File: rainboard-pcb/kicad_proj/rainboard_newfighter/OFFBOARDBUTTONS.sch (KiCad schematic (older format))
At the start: 12 parts, among them J10 Conn_01x02_Female, J11 Conn_01x02_Female, J12 Conn_01x02_Female, J13 Conn_01x02_Female, J14 Conn_01x02_Female, J15 Conn_01x02_Female, J16 Conn_01x02_Female, J17 Conn_01x02_Female, J18 Conn_01x02_Female, J19 Conn_01x02_Female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

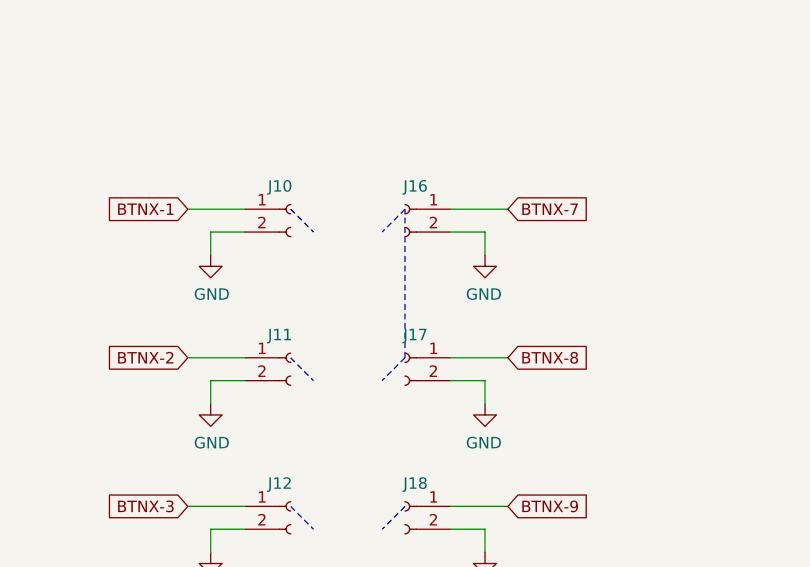
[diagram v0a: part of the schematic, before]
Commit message: Changes Micro USB to USB B
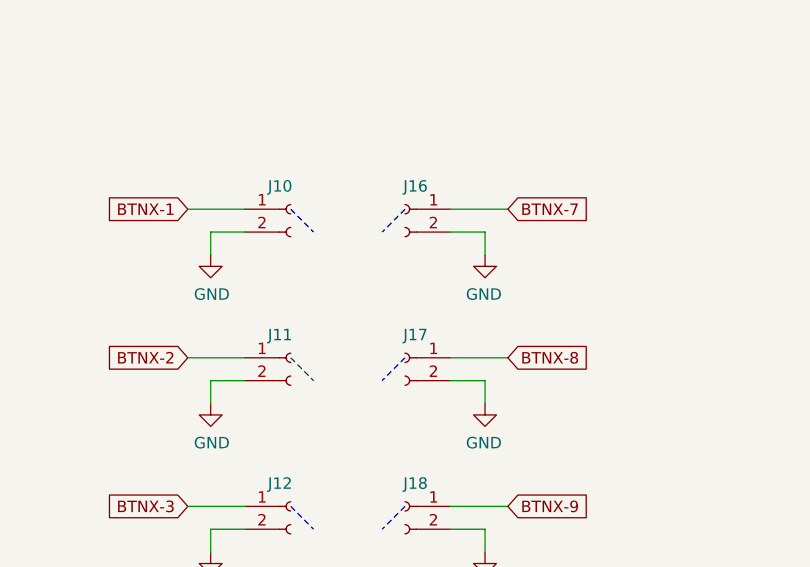
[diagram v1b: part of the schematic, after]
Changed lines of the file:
@@
 Wire Notes Line
 	2650 5750 2550 5850
-Wire Notes Line
-	2650 3150 2650 2500
 $EndSCHEMATC

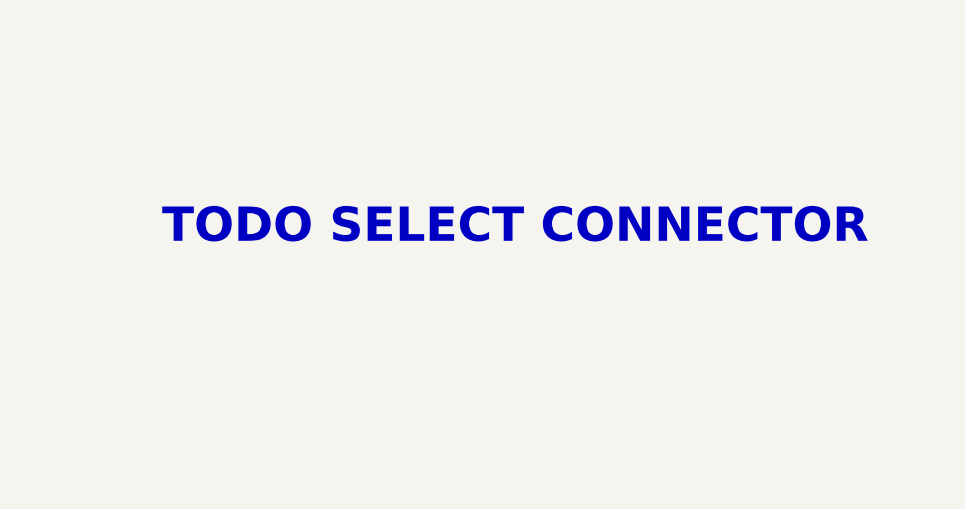
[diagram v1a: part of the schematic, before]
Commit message: Removed RGB from buttons, part numbers updated, cleaned up schematic
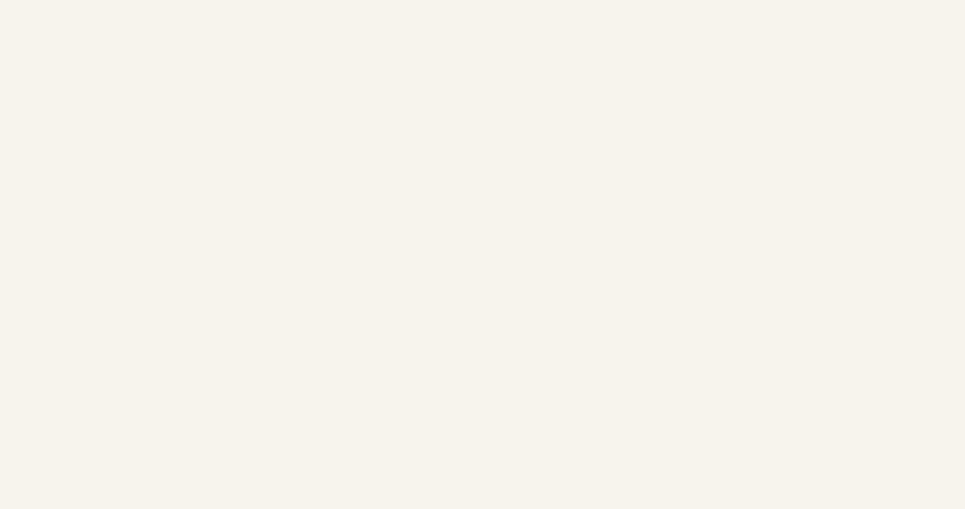
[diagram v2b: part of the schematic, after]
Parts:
- J10, J11, J12, J13, J14, J15, J16, J17, J18, J19, J20, J21: PN (none) -> B2B-XH-A(LF)(SN)
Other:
- note removed: "TODO SELECT CONNECTOR\n"
